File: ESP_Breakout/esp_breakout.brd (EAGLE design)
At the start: 58.4 x 26.3 mm, 12 parts

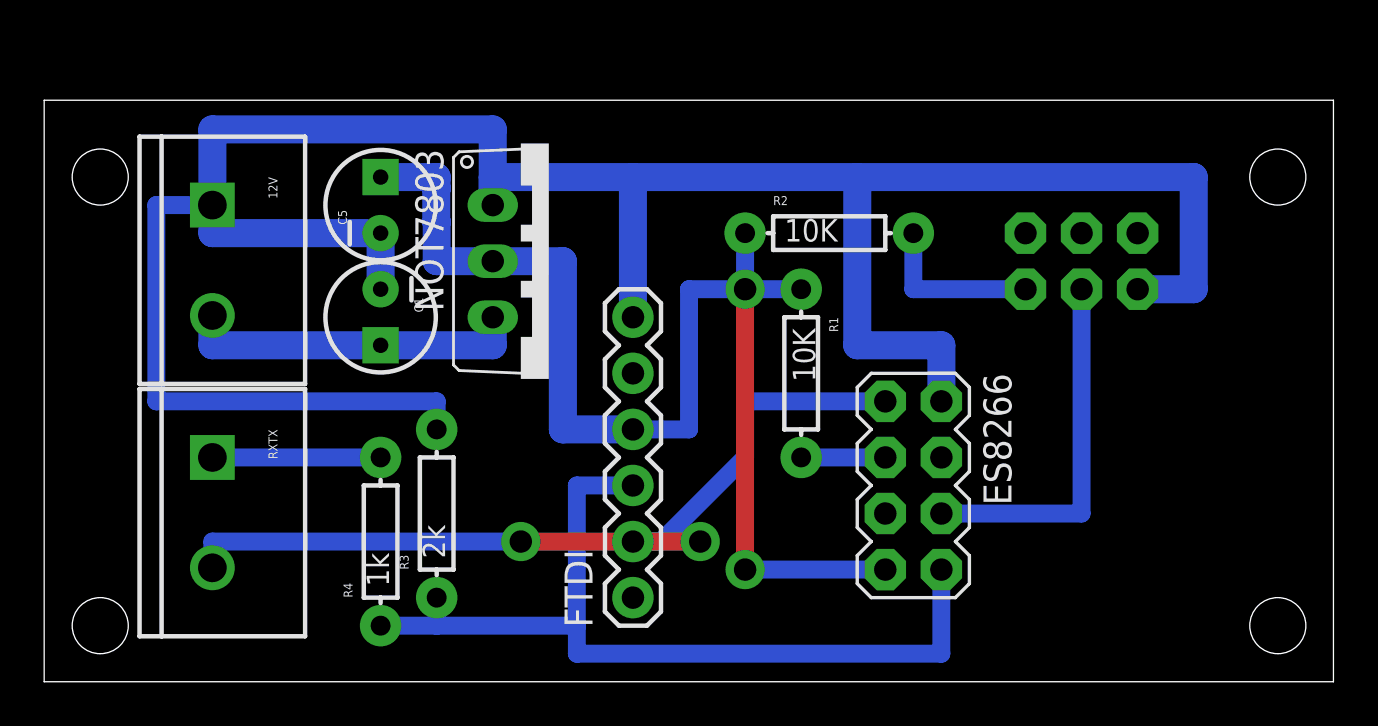
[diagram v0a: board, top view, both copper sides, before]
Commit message: Added breakout board for connecting ESP to AVR
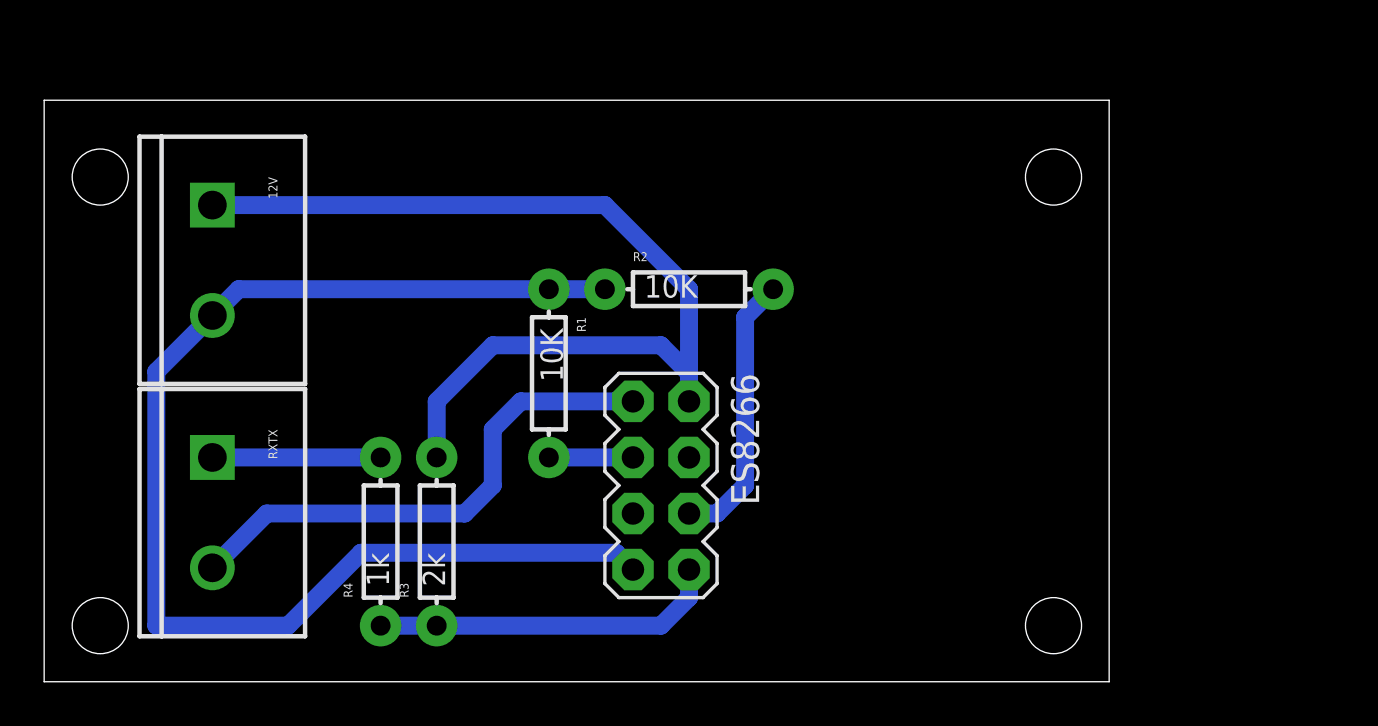
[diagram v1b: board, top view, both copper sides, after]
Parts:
- removed C1: 10uf, SparkFun-Capacitors:CPOL-RADIAL-10UF-25V
- removed C5: 1uf, SparkFun-Capacitors:CPOL-RADIAL-10UF-25V
- removed FTDI: (no value), SparkFun-Connectors:1X06
- removed NOT7803: 7805TV, linear:TO220V
- removed SWITCH1: SWITCH, SparkFun-Connectors:2X3
- moved R1 11.4 mm to (22.9, 14.0)
- moved ES8266 11.4 mm to (27.9, 8.89)
- moved R2 6.84 mm to (29.2, 17.8)
- moved R3 1.27 mm to (17.8, 6.35)
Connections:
- removed net 12V: 12V.2, C1.1, NOT7803.3
- removed net CTS: FTDI.5
- removed net DTR: FTDI.1
- removed net N$2: R2.P$2, SWITCH1.2
- net GND: no longer C1.2, C5.2, FTDI.6, NOT7803.1, SWITCH1.6
- net GPIO0: now also R2.P$2; no longer SWITCH1.4
- net RX: no longer FTDI.2
- net TX: no longer FTDI.3
- net VCC: now also 12V.2; no longer C5.1, FTDI.4, NOT7803.2
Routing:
- net GND: track 117.3 -> 45.1 mm
- net TX: track 40.6 -> 15.8 mm
- net RX: track 41.9 -> 23.7 mm, vias 2 -> 0
- net 12V: track 15.3 -> 0.00 mm
- net N$2: track 7.62 -> 0.00 mm
- net GPIO0: track 16.5 -> 12.5 mm
- net VCC: track 58.4 -> 56.6 mm, vias 2 -> 0
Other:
- board size 58.4 x 26.3 mm -> 48.2 x 26.3 mm

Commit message: Updated ESP8266 module board for connecting to an MCU
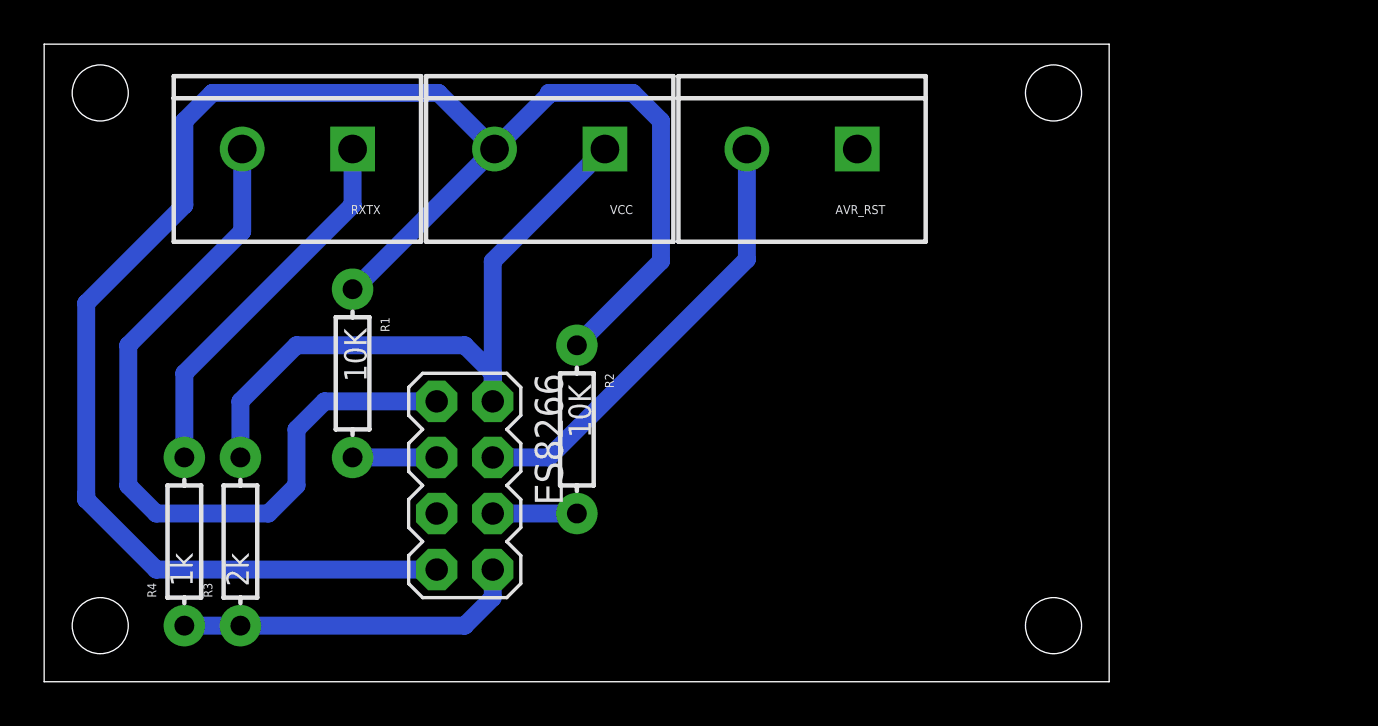
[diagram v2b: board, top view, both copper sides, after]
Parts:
- removed 12V: M025MM, SparkFun-Connectors:SCREWTERMINAL-5MM-2
- added AVR_RST, VCC: M025MM, SparkFun-Connectors:SCREWTERMINAL-5MM-2
- moved RXTX 15.3 mm to (14.0, 24.1), turned to 180 degrees
- moved ES8266 8.89 mm to (19.1, 8.89)
- moved R3 8.89 mm to (8.89, 6.35)
- moved R4 8.89 mm to (6.35, 6.35)
- moved R1 8.89 mm to (14.0, 14.0)
- moved R2 8.13 mm to (24.1, 11.4), turned to 270 degrees
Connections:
- removed net GPIO2: ES8266.4
- new net AVR_RST: AVR_RST.2, ES8266.4
- new net NA: AVR_RST.1
- net GND: now also VCC.1; no longer 12V.1
- net VCC: now also VCC.2; no longer 12V.2
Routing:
- net VCC: track 56.6 -> 82.0 mm
- net AVR_RST: track 0.00 -> 20.2 mm
- net GND: track 45.1 -> 30.4 mm
- net RX: track 23.7 -> 35.5 mm
- net N$1: track 7.62 -> 17.1 mm
- net GPIO0: track 12.5 -> 3.81 mm
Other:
- board size 48.2 x 26.3 mm -> 48.2 x 28.9 mm
